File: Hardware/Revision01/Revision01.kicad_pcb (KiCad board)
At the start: 4 copper layers, 100 x 119.8 mm, 86 parts, among them J1 Battery connector, J2 StrainConn, J3 StrainConn, J4 StrainConn, J5 StrainConn, J6 StrainConn, J7 StrainConn, J8 StrainConn, J9 StrainConn, Q1 PMOS, Q2 NMOS, Q3 PMOS, SW1 StartStop_Push, SW2 ON/OFF_SW_SPST_LED, U1 NCP1117LPST50T3G, U2 NUCLEO-L476RG, U3 LP5813BDRRR, U4 MRF89XAM9AT-I/RM, U5 ICM-45605

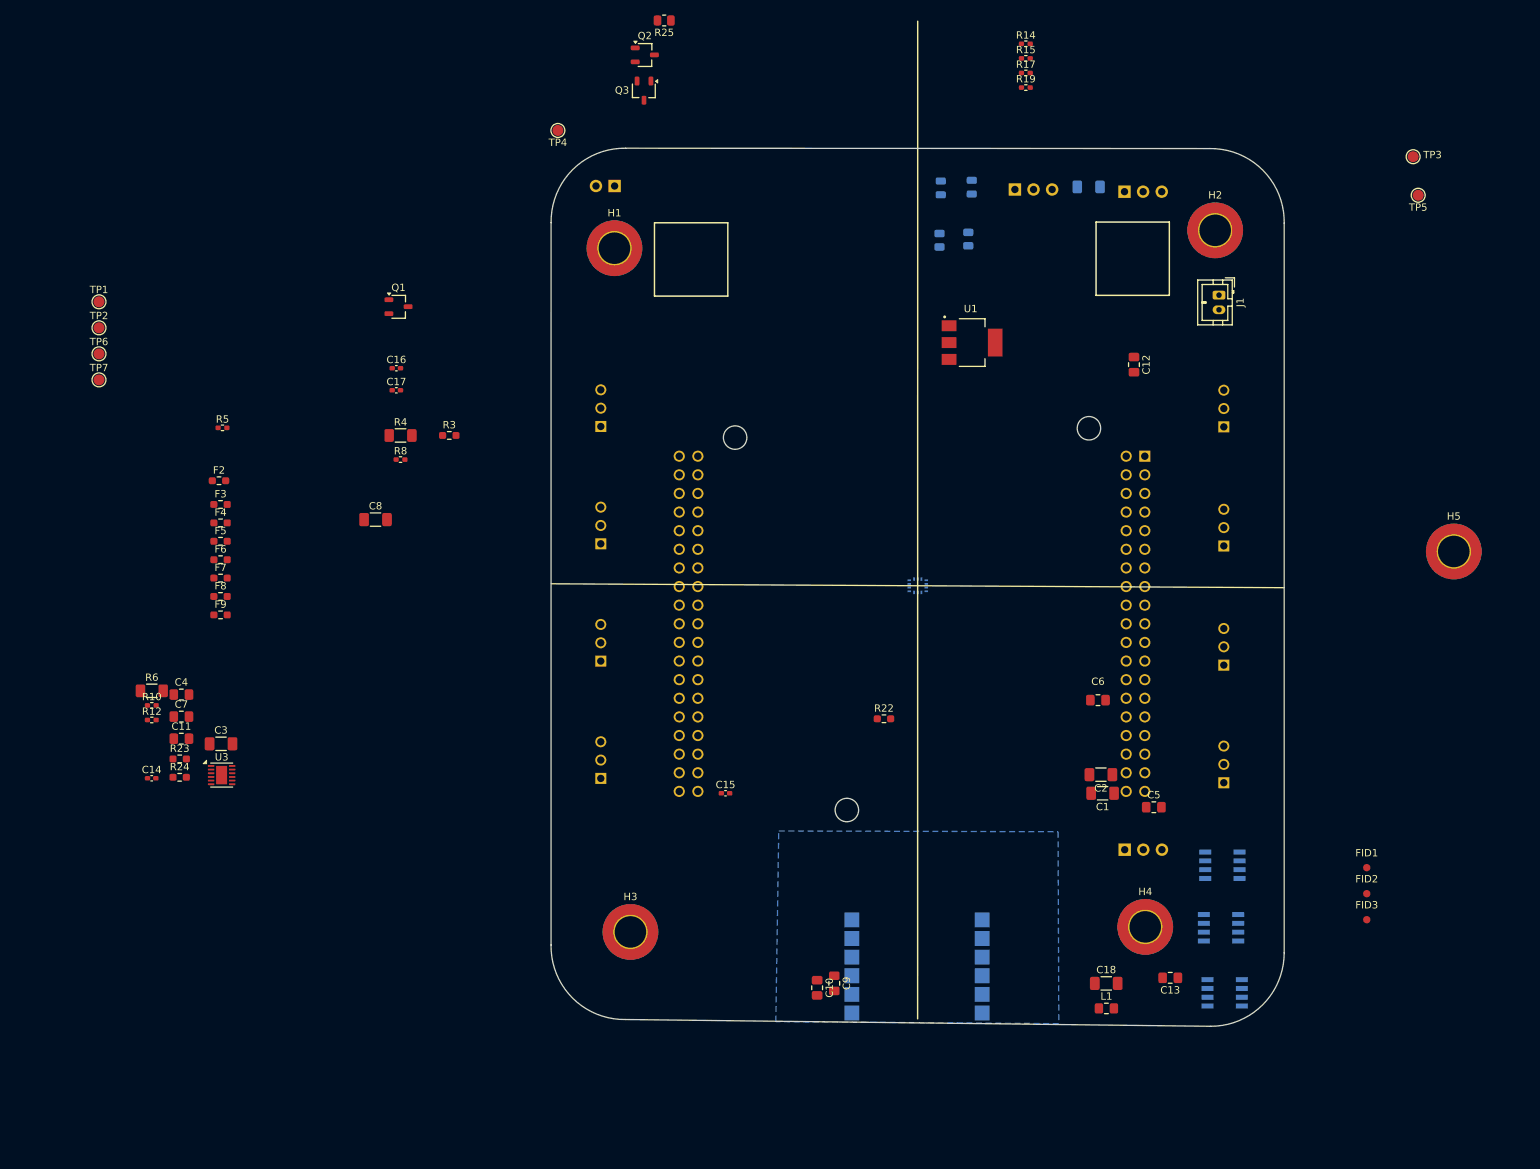
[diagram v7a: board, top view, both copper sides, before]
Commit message: Schematic small details, and beginning wiring
Placed capacitors( in correct polarity)
Branch fuses should be put on the branches(sensor Amplifiers) - as they protect branches
Added Main fuse(protecting main circuit - from connector)
Changed all component sizes back to 0805 atleast
Started PCB WIRING
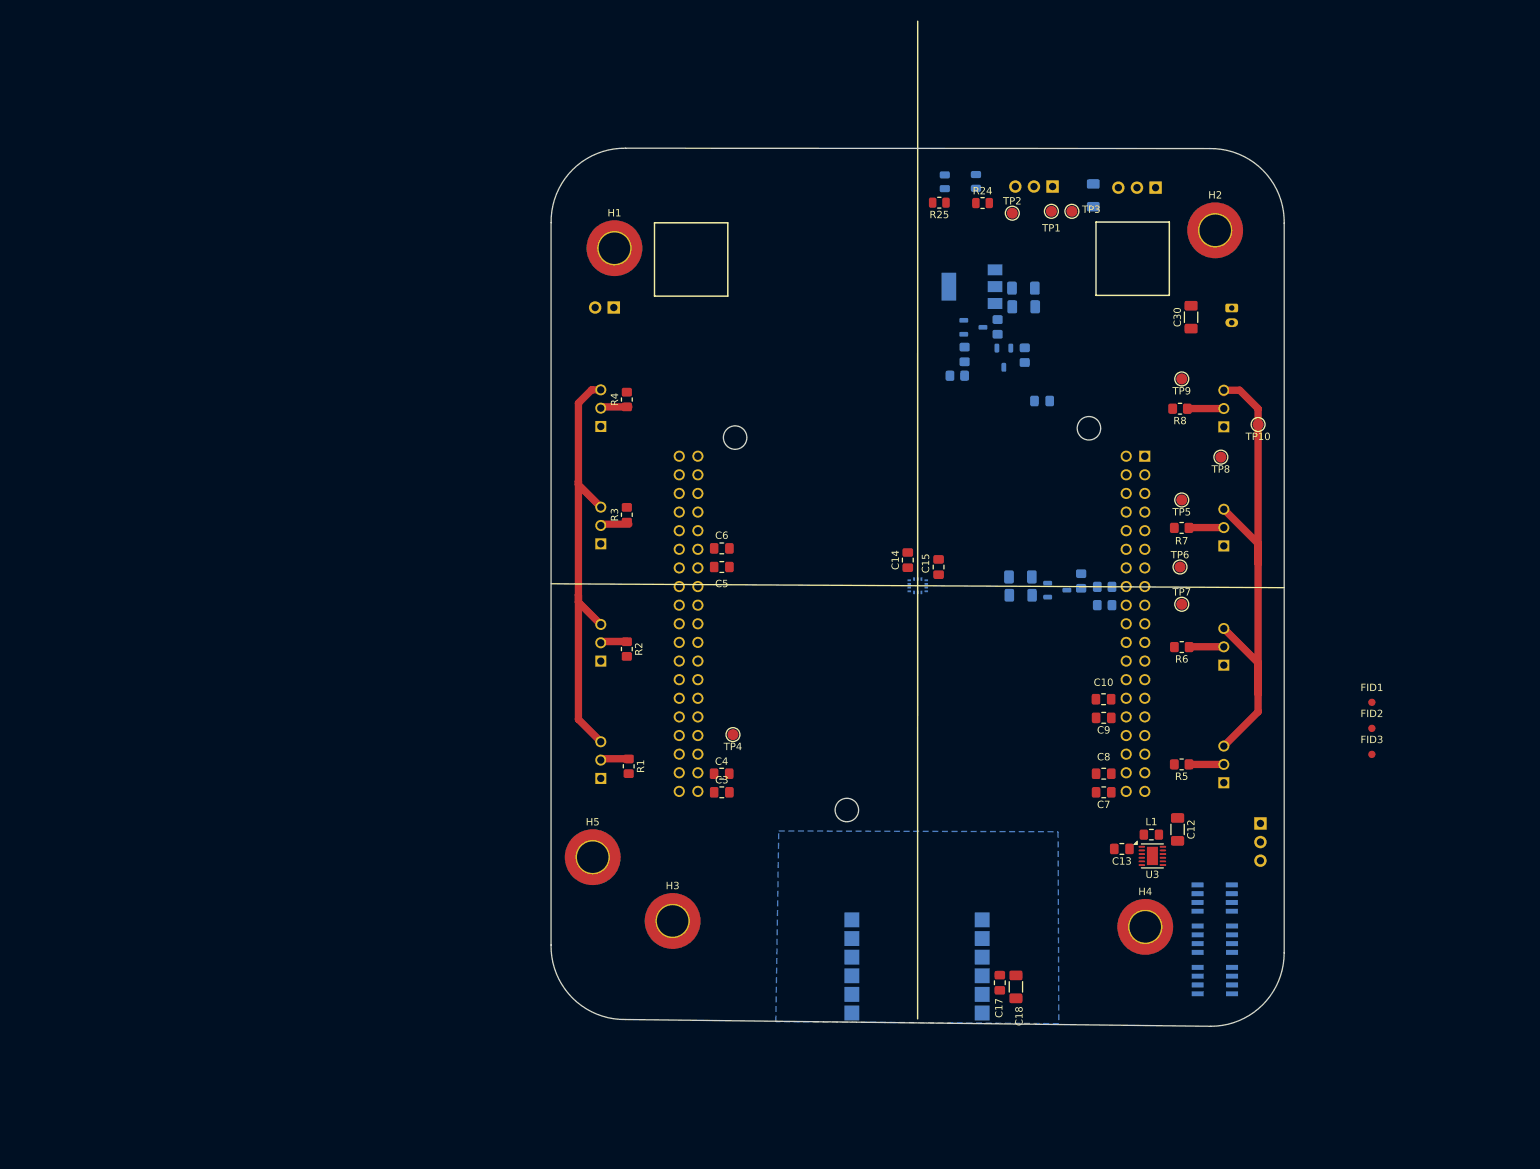
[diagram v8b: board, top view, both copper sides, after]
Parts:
- removed F2, F3, F4, F5, F6, F7, F8, F9: Polyfuse_Small, Resistor_SMD:R_0603_1608Metric_Pad0.98x0.95mm_HandSolder
- removed R12, R14, R15, R17, R19: 1.6K +-1%, Resistor_SMD:R_0402_1005Metric_Pad0.72x0.64mm_HandSolder
- added C30: 10uF, Capacitor_SMD:C_1206_3216Metric_Pad1.33x1.80mm_HandSolder, F.Cu at (198.3, 56.0)
- added F10: 125mA hold, 290mA trip, Resistor_SMD:R_1206_3216Metric_Pad1.30x1.75mm_HandSolder, B.Cu at (175.1, 93.9)
- added R11: 0K +-1%, Resistor_SMD:R_0805_2012Metric_Pad1.20x1.40mm_HandSolder, B.Cu at (186.5, 92.8)
- added R20: 10K +-1%, Resistor_SMD:R_0805_2012Metric_Pad1.20x1.40mm_HandSolder, B.Cu at (175.6, 61.2)
- added R21: 10K +-1%, Resistor_SMD:R_0805_2012Metric_Pad1.20x1.40mm_HandSolder, B.Cu at (171.9, 57.3)
- added R7: 1.6K +-1%, Resistor_SMD:R_0805_2012Metric_Pad1.20x1.40mm_HandSolder, F.Cu at (197.0, 84.7)
- added R9: 10K +-1%, Resistor_SMD:R_0805_2012Metric_Pad1.20x1.40mm_HandSolder, B.Cu at (183.3, 92.0)
- added TP10: TestPoint, TestPoint:TestPoint_Pad_D1.5mm, F.Cu at (207.5, 70.6)
- added TP8: TestPoint, TestPoint:TestPoint_Pad_D1.5mm, F.Cu at (202.4, 75.1)
- added TP9: TestPoint, TestPoint:TestPoint_Pad_D1.5mm, F.Cu at (197.1, 64.4)
- C1, C2, J1, Q1, Q2, Q3, U1: moved to B.Cu
- C11: value 10nF -> 100uF; footprint Capacitor_SMD:C_0805_2012Metric_Pad1.18x1.45mm_HandSolder -> Capacitor_SMD:C_1206_3216Metric_Pad1.33x1.80mm_HandSolder; moved to B.Cu
- C12: value 10nF -> 10uF; footprint Capacitor_SMD:C_0805_2012Metric_Pad1.18x1.45mm_HandSolder -> Capacitor_SMD:C_1206_3216Metric_Pad1.33x1.80mm_HandSolder
- C14, C15, C17: footprint Capacitor_SMD:C_0402_1005Metric_Pad0.74x0.62mm_HandSolder -> Capacitor_SMD:C_0805_2012Metric_Pad1.18x1.45mm_HandSolder
- C16: footprint Capacitor_SMD:C_0402_1005Metric_Pad0.74x0.62mm_HandSolder -> Capacitor_SMD:C_0805_2012Metric_Pad1.18x1.45mm_HandSolder; moved to B.Cu
- C3: value 100uF -> 10nF; footprint Capacitor_SMD:C_1206_3216Metric_Pad1.33x1.80mm_HandSolder -> Capacitor_SMD:C_0805_2012Metric_Pad1.18x1.45mm_HandSolder
- C8: value 10uF -> 10nF; footprint Capacitor_SMD:C_1206_3216Metric_Pad1.33x1.80mm_HandSolder -> Capacitor_SMD:C_0805_2012Metric_Pad1.18x1.45mm_HandSolder
- D1: value BLUE LED -> Indicication_RGB_Led; footprint LED_SMD:LED_0805_2012Metric -> Connector_PinHeader_2.54mm:PinHeader_1x03_P2.54mm_Vertical
- D2: value RED LED -> RGBW_LED; footprint LED_SMD:LED_0805_2012Metric -> RGBW:SOL120P540X160-8N
- D3: value Indicication_RGB_Led -> RGBW_LED; footprint Connector_PinHeader_2.54mm:PinHeader_1x03_P2.54mm_Vertical -> RGBW:SOL120P540X160-8N
- D5: value RGBW_LED -> BLUE LED; footprint RGBW:SOL120P540X160-8N -> LED_SMD:LED_0805_2012Metric
- D6: value RGBW_LED -> RED LED; footprint RGBW:SOL120P540X160-8N -> LED_SMD:LED_0805_2012Metric
- R1, R2: value 330 +-5% -> 1.6K +-1%; footprint Resistor_SMD:R_0805_2012Metric -> Resistor_SMD:R_0805_2012Metric_Pad1.20x1.40mm_HandSolder; moved to F.Cu
- R10: value 1.6K +-1% -> 0K +-1%; footprint Resistor_SMD:R_0402_1005Metric_Pad0.72x0.64mm_HandSolder -> Resistor_SMD:R_0805_2012Metric_Pad1.20x1.40mm_HandSolder; moved to B.Cu
- R22: value 10K +-1% -> 15K +-1%; footprint Resistor_SMD:R_0603_1608Metric_Pad0.98x0.95mm_HandSolder -> Resistor_SMD:R_0805_2012Metric_Pad1.20x1.40mm_HandSolder; moved to B.Cu
- R23: value 10K +-1% -> 3.3K +-1%; footprint Resistor_SMD:R_0603_1608Metric_Pad0.98x0.95mm_HandSolder -> Resistor_SMD:R_0805_2012Metric_Pad1.20x1.40mm_HandSolder; moved to B.Cu
- R24: value 15K +-1% -> 330 +-5%; footprint Resistor_SMD:R_0603_1608Metric_Pad0.98x0.95mm_HandSolder -> Resistor_SMD:R_0805_2012Metric
- R25: value 3.3K +-1% -> 330 +-5%
- R3: value 10K +-1% -> 1.6K +-1%; footprint Resistor_SMD:R_0603_1608Metric_Pad0.98x0.95mm_HandSolder -> Resistor_SMD:R_0805_2012Metric_Pad1.20x1.40mm_HandSolder
- R4, R6: value 0K +-1% -> 1.6K +-1%; footprint Resistor_SMD:R_1206_3216Metric_Pad1.30x1.75mm_HandSolder -> Resistor_SMD:R_0805_2012Metric_Pad1.20x1.40mm_HandSolder
- R5, R8: footprint Resistor_SMD:R_0402_1005Metric_Pad0.72x0.64mm_HandSolder -> Resistor_SMD:R_0805_2012Metric_Pad1.20x1.40mm_HandSolder
- moved TP7 150.8 mm to (197.1, 95.2)
- moved TP6 150.3 mm to (196.8, 90.1)
- moved R6 140.6 mm to (197.1, 101.0), turned to 180 degrees
- moved R5 138.6 mm to (197.0, 117.0), turned to 180 degrees
- moved R24 134.6 mm to (169.9, 40.4)
- moved R10 130.7 mm to (186.5, 95.3)
- moved TP1 130.5 mm to (179.3, 41.6)
- moved U3 127.4 mm to (193.0, 129.5)
- moved C7 126.2 mm to (186.4, 120.8), turned to 180 degrees
- moved TP2 125.6 mm to (173.9, 41.8)
- moved H5 124.6 mm to (116.7, 129.7)
- moved R23 118.2 mm to (166.4, 64.0)
- moved D6 117.0 mm to (164.7, 37.5), turned to 90 degrees
- moved C11 116.6 mm to (175.0, 91.4)
- moved C17 115.3 mm to (172.2, 146.8), turned to -90 degrees
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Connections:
- C10 pad 1: /AIN_6 -> /AIN1_6
- C11 pad 1: /AIN_7 -> /Application/+StrainV
- C12 pad 1: /AIN_8 -> +3.3V
- C16 pad 1: /BatteryV_AIN -> /BatteryV_AIN2
- C3 pad 1: /Application/+StrainV -> /AIN1_8
- C4 pad 1: /AIN_1 -> /AIN1_7
- C5 pad 1: /AIN_2 -> /AIN1_11
- C6 pad 1: /AIN_3 -> /AIN1_10
- C7 pad 1: /AIN_4 -> /AIN1_1
- C8 pad 1: +3.3V -> /AIN1_2
- C9 pad 1: /AIN_5 -> /AIN1_5
- D1 pad 1: Net-(D1-K) -> /Application/U1_OUT1
- D1 pad 2: +5V_USB -> /Application/U1_OUT2
- D2 pad 1: Net-(D2-K) -> /Application/U1_OUT1
- D2 pad 2: +3.3V -> /Application/U1_OUT2
- D3 pad 1: /Application/U1_OUT1 -> /Application/U1_OUT2
- D3 pad 2: /Application/U1_OUT2 -> /Application/U1_OUT3
- D3 pad 3: /Application/U1_OUT3 -> /Application/U1_OUT0
- D4 pad 1: /Application/U1_OUT1 -> /Application/U1_OUT3
- D4 pad 2: /Application/U1_OUT2 -> /Application/U1_OUT0
- D4 pad 3: /Application/U1_OUT3 -> /Application/U1_OUT1
- D4 pad 4: /Application/U1_OUT0 -> /Application/U1_OUT2
- D5 pad 1: /Application/U1_OUT2 -> /USB_5V_GPIO_EN
- D5 pad 2: /Application/U1_OUT3 -> +5V_USB
- D6 pad 1: /Application/U1_OUT3 -> Net-(D6-K)
- D6 pad 2: /Application/U1_OUT0 -> +3.3V
- J2 pad 3: Net-(J2-Pin_3) -> /Application/+StrainV
- J3 pad 3: Net-(J3-Pin_3) -> /Application/+StrainV
- J4 pad 3: Net-(J4-Pin_3) -> /Application/+StrainV
- J5 pad 3: Net-(J5-Pin_3) -> /Application/+StrainV
- J6 pad 3: Net-(J6-Pin_3) -> /Application/+StrainV
- J7 pad 3: Net-(J7-Pin_3) -> /Application/+StrainV
- J8 pad 3: Net-(J8-Pin_3) -> /Application/+StrainV
- J9 pad 3: Net-(J9-Pin_3) -> /Application/+StrainV
- Q1 pad 1: /Application/+StrainV -> Net-(Q1-D)
- R1 pad 1: Net-(D1-K) -> /Application/OpAmpOutput1
- R1 pad 2: Earth -> /AIN1_8
- R10 pad 1: /Application/OpAmpOutput3 -> Net-(Q1-S)
- R10 pad 2: /AIN_3 -> +5V
- R2 pad 1: Net-(D2-K) -> /Application/OpAmpOutput2
- R2 pad 2: Earth -> /AIN1_7
- R22 pad 1: Earth -> /BatteryV_AIN2
- R22 pad 2: /BatteryV_Div_Enable_GPIO -> Net-(Q3-D)
- R23 pad 1: Net-(Q2-D) -> Earth
- R23 pad 2: +V_batt -> /BatteryV_AIN2
- R24 pad 1: /BatteryV_AIN -> /USB_5V_GPIO_EN
- R24 pad 2: Net-(Q3-D) -> Earth
- R25 pad 1: Earth -> Net-(D6-K)
- R25 pad 2: /BatteryV_AIN -> Earth
- R3 pad 1: /StrainV_Enable_GPIO -> /Application/OpAmpOutput3
- R3 pad 2: Net-(Q1-S) -> /AIN1_11
- R4 pad 1: Net-(Q1-S) -> /Application/OpAmpOutput4
- R4 pad 2: +5V -> /AIN1_10
- R5 pad 1: /Application/OpAmpOutput1 -> /Application/OpAmpOutput5
- R5 pad 2: /AIN_1 -> /AIN1_1
- R6 pad 1: Net-(Q1-S) -> /Application/OpAmpOutput6
- R6 pad 2: +3.3V -> /AIN1_2
- R8 pad 1: /Application/OpAmpOutput2 -> /Application/OpAmpOutput8
- R8 pad 2: /AIN_2 -> /AIN1_6
- SW1 pad 2: Earth -> +3.3V
- U2 pad CN10_11: /ANT_CSCON_GPIO -> /AIN1_10
- U2 pad CN10_13: /ANT_CSDATA_GPIO -> /AIN1_11
- U2 pad CN10_15: /ANT_IRQ0_GPIO -> unconnected-(U2B-PA7-PadCN10_15)
- U2 pad CN10_17: /ANT_IRQ1_GPIO -> unconnected-(U2B-PB6-PadCN10_17)
- U2 pad CN10_19: /ANT_RESET_ANT_GPIO -> unconnected-(U2B-PC7-PadCN10_19)
- U2 pad CN10_21: /STARTSTOP_GPIO -> unconnected-(U2B-PA9-PadCN10_21)
- U2 pad CN10_29: /Vref+ -> unconnected-(U2B-PB5-PadCN10_29)
- U2 pad CN10_35: /AIN_7 -> /AIN1_7
- U2 pad CN10_37: /AIN_8 -> /AIN1_8
- U2 pad CN7_28: /AIN_5 -> /AIN1_6
- U2 pad CN7_30: /AIN_6 -> /AIN1_5
- U2 pad CN7_32: /BatteryV_AIN -> unconnected-(U2A-PA4-PadCN7_32)
- U2 pad CN7_35: /AIN_3 -> unconnected-(U2A-PC2-PadCN7_35)
- U2 pad CN7_36: /AIN_2 -> /AIN1_2
- U2 pad CN7_37: /AIN_4 -> unconnected-(U2A-PC3-PadCN7_37)
- U2 pad CN7_38: /AIN_1 -> /AIN1_1
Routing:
- net /Application/+StrainV: track 0.00 -> 135.5 mm
- net /Application/OpAmpOutput8: track 0.00 -> 4.98 mm
- net /Application/OpAmpOutput7: track 0.00 -> 4.77 mm
- net /Application/OpAmpOutput5: track 0.00 -> 4.75 mm
- net /Application/OpAmpOutput6: track 0.00 -> 4.75 mm
- net /Application/OpAmpOutput4: track 0.00 -> 3.91 mm
- net /Application/OpAmpOutput3: track 0.00 -> 3.91 mm
- net /Application/OpAmpOutput1: track 0.00 -> 3.64 mm
- net /Application/OpAmpOutput2: track 0.00 -> 3.63 mm
